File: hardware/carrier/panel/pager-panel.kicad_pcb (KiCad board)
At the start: 2 copper layers, 40 x 20 mm, 22 parts, among them J1 GDEY029T94 FPC, J2 CARRIER, Q5 AO3400A

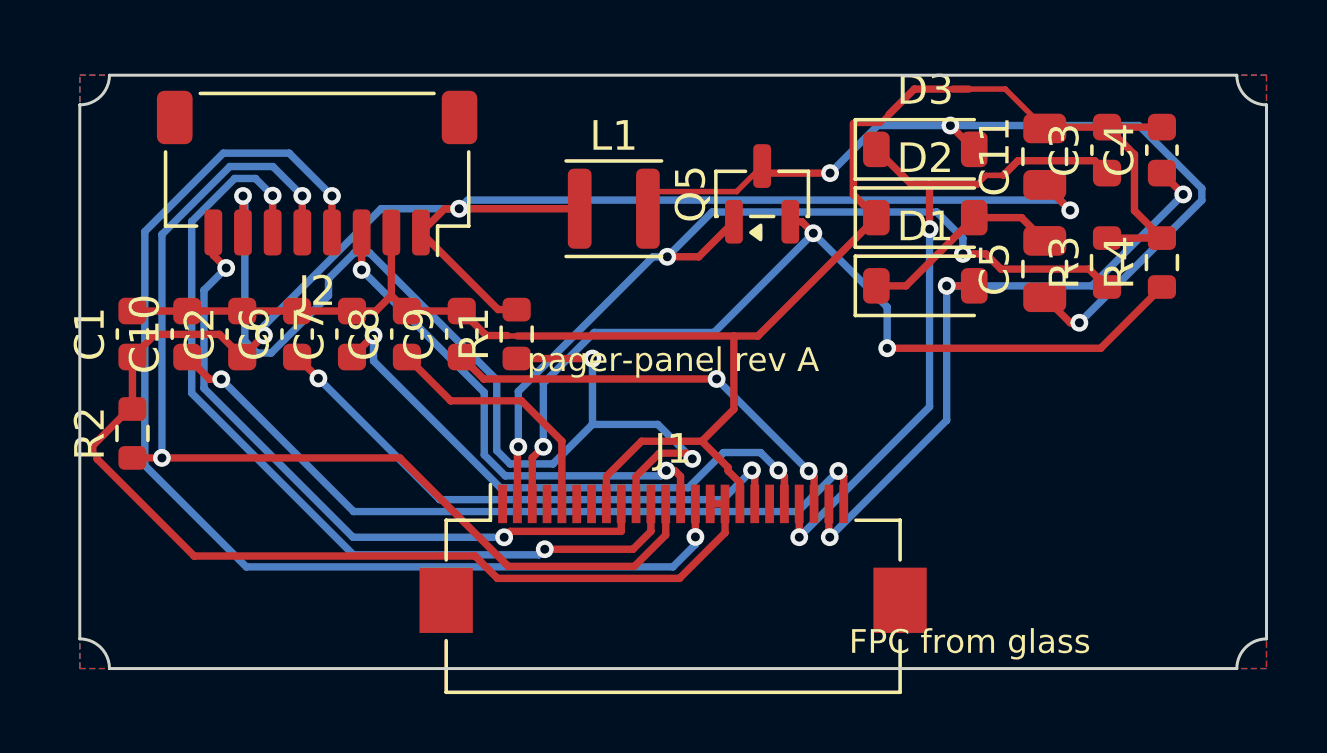
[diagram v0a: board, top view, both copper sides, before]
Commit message: hardware/carrier: route both boards (Freerouting via pcbnew DSN/SES), DRC-fix pass -- NC-pin nets, 1.7 mm Walter pads, edge keep-outs, courtyard and BOM-attribute sync; panel fully routed (silk warnings only), carrier one USB_DM link unrouted plus a few courtyard nits listed in the README; board PDFs exported
Co-Authored-By: Claude Fable 5.1 <noreply@anthropic.com>
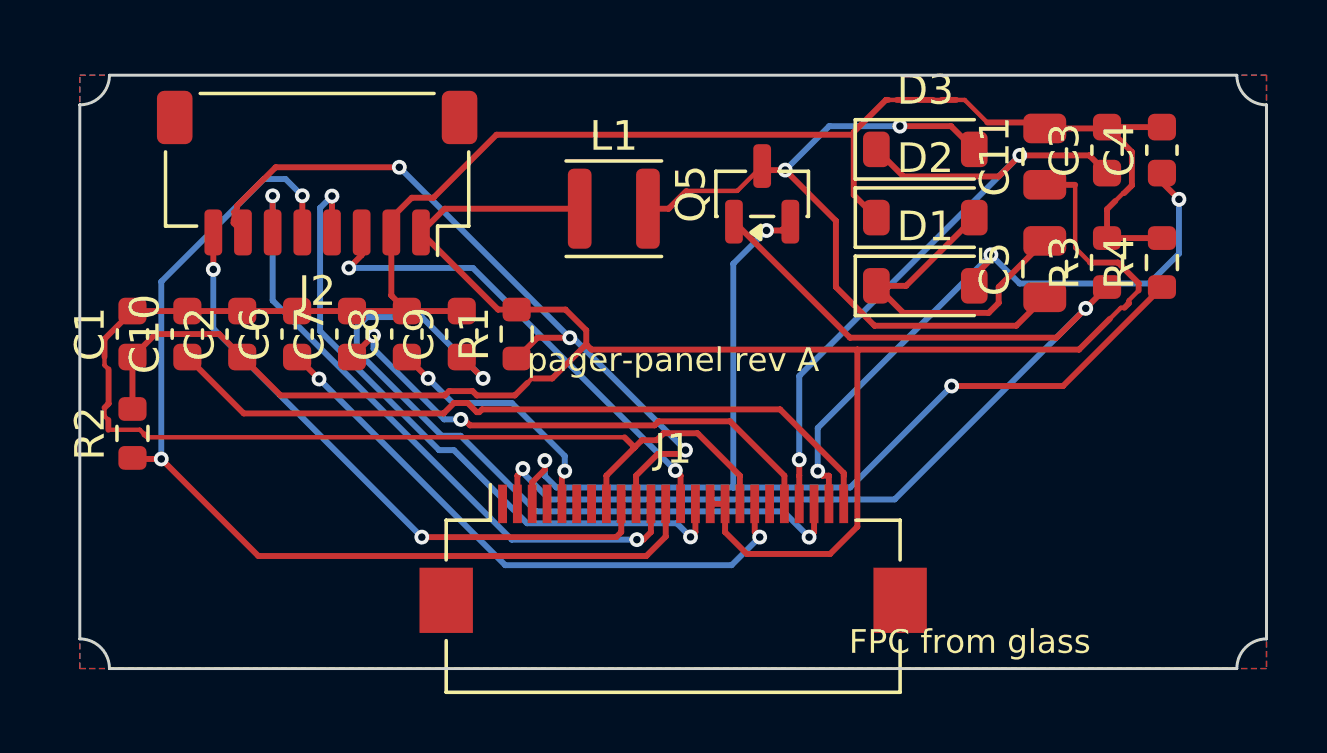
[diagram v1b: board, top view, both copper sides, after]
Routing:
- net GND: track 62.2 -> 82.1 mm
- net EPD_MOSI: track 38.8 -> 22.5 mm
- net EPD_VSL: track 14.5 -> 26.1 mm
- net EPD_RST: track 36.5 -> 25.7 mm
- net EPD_GDR: track 30.2 -> 38.3 mm, vias 3 -> 2
- net EPD_DC: track 29.6 -> 21.9 mm
- net EPD_SW: track 30.1 -> 25.2 mm, vias 3 -> 2
- net EPD_PUMP: track 6.95 -> 11.6 mm
- net 3V3_EPD: track 75.0 -> 70.3 mm, vias 3 -> 0
- net EPD_RESE: track 31.4 -> 36.0 mm
- net EPD_BUSY: track 22.9 -> 20.9 mm
- net EPD_CS: track 35.8 -> 34.4 mm
- net EPD_VDD: track 18.9 -> 20.1 mm
- net EPD_VSH1: track 19.3 -> 18.2 mm
- net EPD_SCK: track 17.2 -> 16.4 mm
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
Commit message: hardware/carrier: front light is the GDEY029T94-FL03 (6-pin flex -> FH34SRJ-6S on the panel board, anode/cathode over a 10-way SH cable, 33R 1206 + Q4 PWM drive replaces the NSI45020), front-light button SW2 on IO4 (FL_BTN), low-profile pass (FH34SRJ 1.0 mm ZIFs, 2 x 100uF 0805 instead of the 2.5 mm 1210, part-height table), sleep-current audit (Q1 gate pull-up 100k -> 2.2M: 38 -> 1.9 uA; SN74LVC2G126 moved to the bus-powered BRG_VDD rail: 0 on battery; table in the README), TPS62840 has no fixed-3.3 V variant (README). Custom FH34SRJ footprints from the Hirose catalog; LCSC numbers via the JLCPCB parts API. Both boards re-placed and re-routed: 0 unconnected, 0 clearance/courtyard errors, silk notes only; ERC 0/0; exports refreshed (owner, 17 Oct 2026)
Co-Authored-By: Claude Fable 5.1 <noreply@anthropic.com>
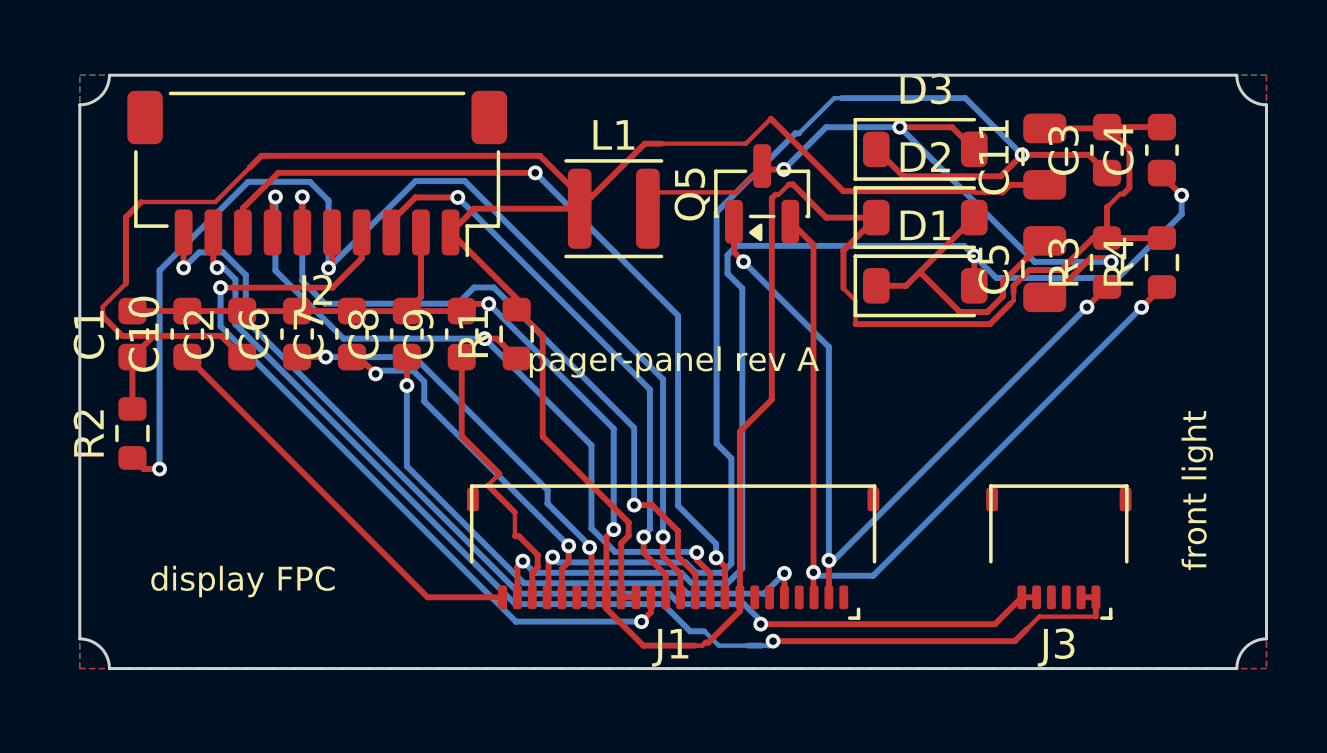
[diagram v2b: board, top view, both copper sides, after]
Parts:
- added J3: FRONTLIGHT FPC, pager-carrier:Hirose_FH34SRJ-6S-0.5SH_1x06-1MP_P0.50mm_Horizontal, F.Cu at (33.0, 17.6)
- J1: footprint Connector_FFC-FPC:Hirose_FH12-24S-0.5SH_1x24-1MP_P0.50mm_Horizontal -> pager-carrier:Hirose_FH34SRJ-24S-0.5SH_1x24-1MP_P0.50mm_Horizontal
- J2: footprint Connector_JST:JST_SH_SM08B-SRSS-TB_1x08-1MP_P1.00mm_Horizontal -> Connector_JST:JST_SH_SM10B-SRSS-TB_1x10-1MP_P1.00mm_Horizontal
- moved J1 1.30 mm to (20.0, 17.6), turned to 180 degrees
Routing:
- net FL_ANODE: track 0.00 -> 38.6 mm, vias 0 -> 2
- net FL_CATHODE: track 0.00 -> 36.7 mm, vias 0 -> 2
- net EPD_VGH: track 23.5 -> 41.2 mm
- net EPD_VGL: track 22.5 -> 39.4 mm
- net EPD_VSL: track 26.1 -> 9.64 mm, vias 2 -> 0
- net EPD_VCOM: track 25.2 -> 14.0 mm
- net EPD_GDR: track 38.3 -> 27.2 mm, vias 2 -> 3
- net EPD_VSH2: track 8.36 -> 19.3 mm
- net EPD_BUSY: track 20.9 -> 28.1 mm
- net EPD_RESE: track 36.0 -> 28.8 mm, vias 3 -> 2
- net EPD_CS: track 34.4 -> 41.3 mm, vias 2 -> 3
- net GND: track 82.1 -> 75.5 mm, vias 0 -> 2
- net EPD_VSH1: track 18.2 -> 12.2 mm
- net EPD_VDD: track 20.1 -> 14.5 mm
- net EPD_MOSI: track 22.5 -> 26.6 mm
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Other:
- board text added: "display FPC"
- board text added: "front light"
- board text removed: "FPC from glass"
